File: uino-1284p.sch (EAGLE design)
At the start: 59 parts, among them J1 POWER, J2 POWER_JACKPTH, J3 M03X2, J4 POWER_SELECT, J5 M03X2, J6 IO, J7 ANALOG, J8 IOL, J9 IOH, U1 LD117AS50TR, U2 ATMEGA1284AU, U3 ATMEGA8U2AU, X1 16MHz, X2 16MHz

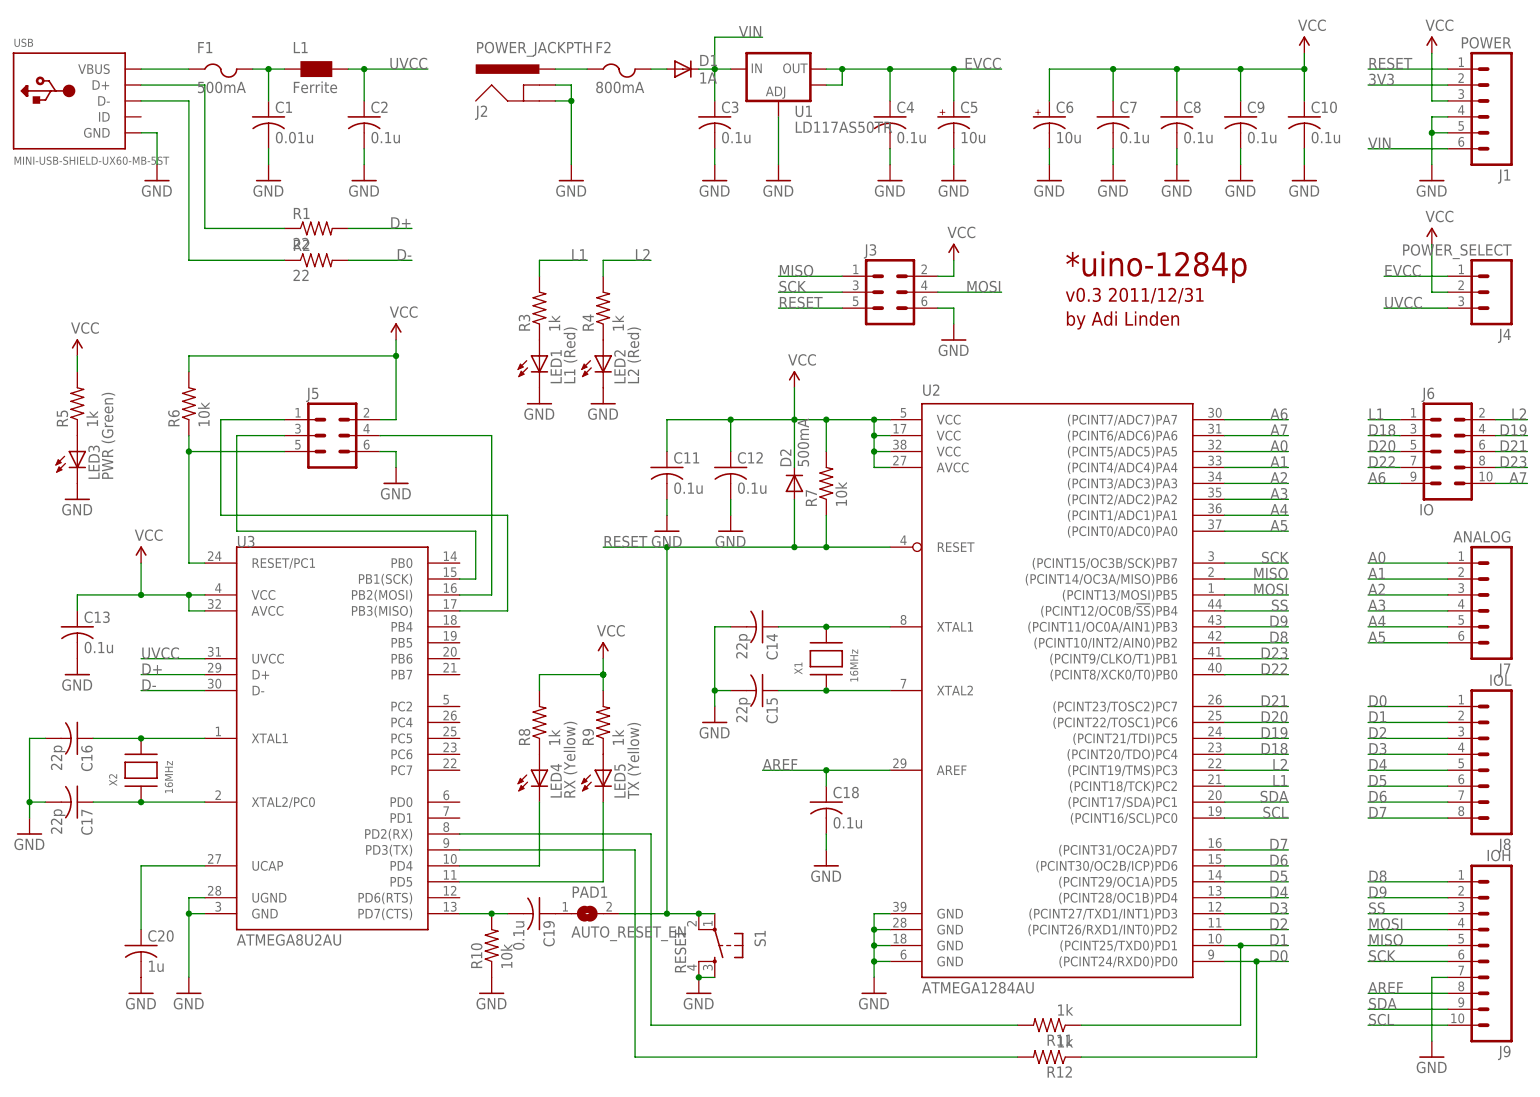
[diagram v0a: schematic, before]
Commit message: Unified device name text on board. Arranged name labels.
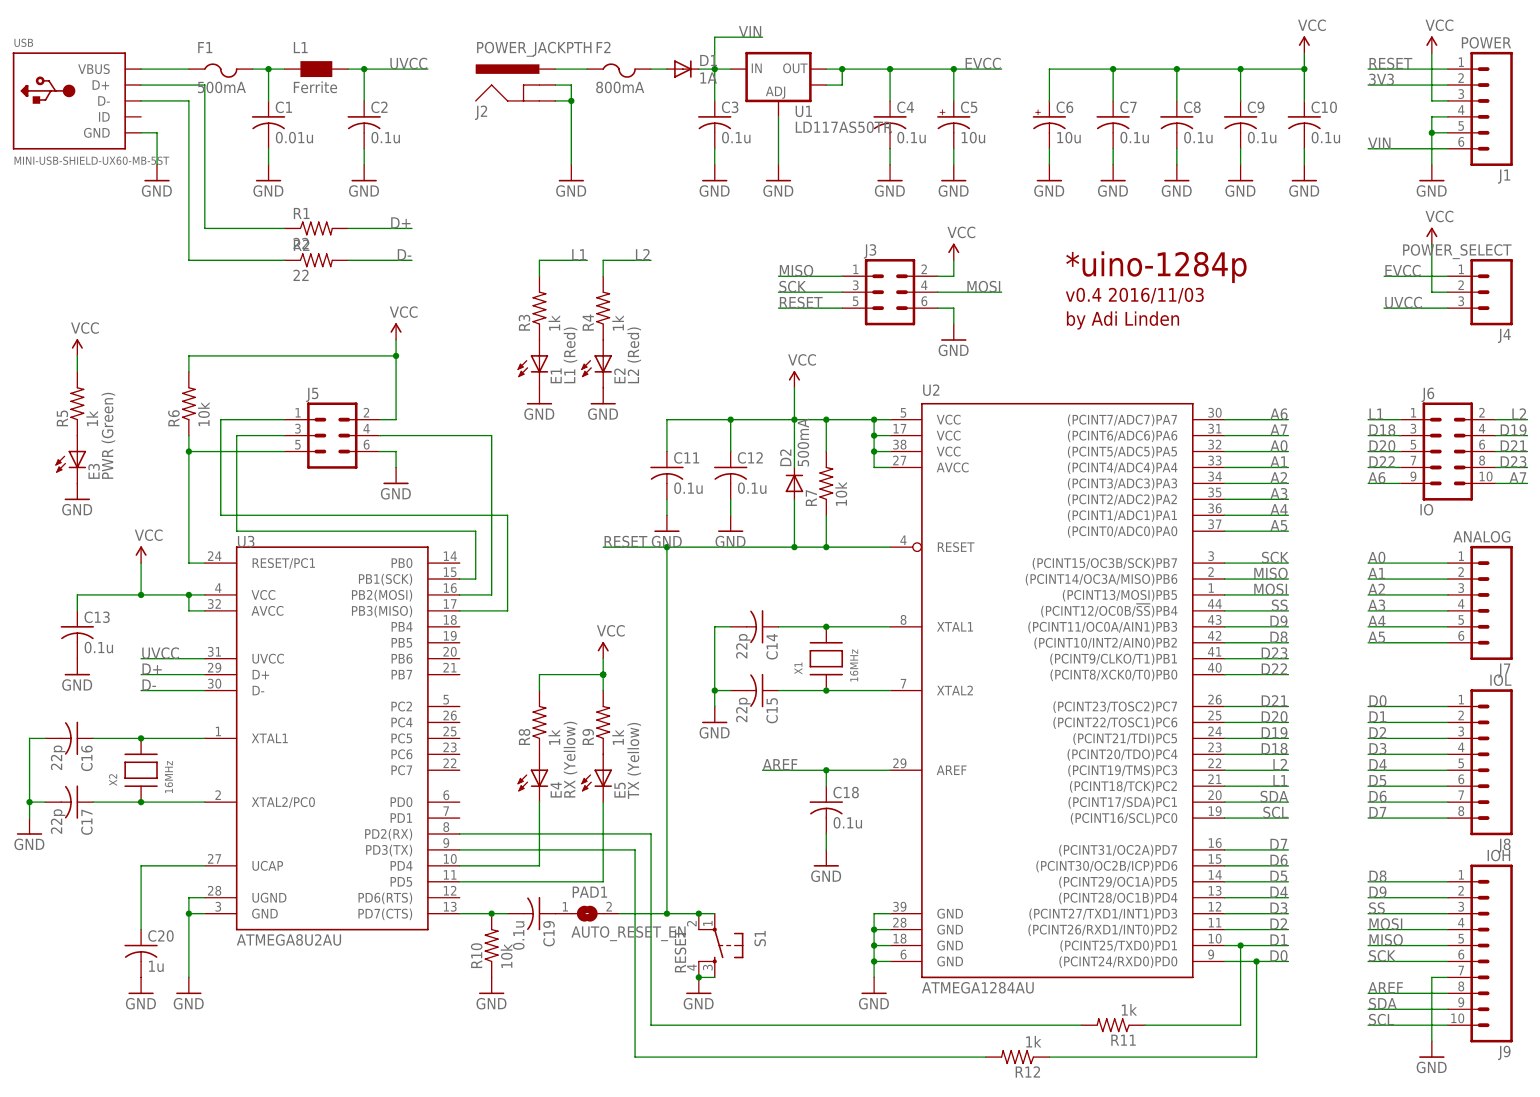
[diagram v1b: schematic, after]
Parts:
- renumbered LED1 to E1, LED2 to E2, LED3 to E3, LED4 to E4, LED5 to E5
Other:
- note added: "v0.4 2016/11/03"
- note removed: "v0.3 2011/12/31"
- moved on the sheet: R11, R12
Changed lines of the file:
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@@
 <setting verticaltext="up"/>
 </settings>
-<grid distance="0.1" unitdist="inch" unit="inch" style="lines" multiple="1" display="yes" altdistance="0.01" altunitdist="inch" altunit="inch"/>
+<grid distance="0.1" unitdist="inch" unit="inch" style="lines" multiple="1" display="no" altdistance="0.01" altunitdist="inch" altunit="inch"/>
 <layers>
 <layer number="1" name="Top" color="4" fill="1" visible="no" active="no"/>
@@
 <part name="P+3" library="SparkFun" deviceset="VCC" device=""/>
 <part name="GND12" library="supply1" deviceset="GND" device=""/>
-<part name="LED4" library="adafruit" deviceset="LED" device="CHIP-LED0805" value="RX (Yellow)"/>
-<part name="LED5" library="adafruit" deviceset="LED" device="CHIP-LED0805" value="TX (Yellow)"/>
+<part name="E4" library="adafruit" deviceset="LED" device="CHIP-LED0805" value="RX (Yellow)"/>
+<part name="E5" library="adafruit" deviceset="LED" device="CHIP-LED0805" value="TX (Yellow)"/>
 <part name="R8" library="rcl" deviceset="R-US_" device="R0805" value="1k"/>
 <part name="R9" library="rcl" deviceset="R-US_" device="R0805" value="1k"/>
@@
 <part name="C5" library="rcl" deviceset="CPOL-US" device="CT3216" value="10u"/>
 <part name="R5" library="rcl" deviceset="R-US_" device="R0805" value="1k"/>
-<part name="LED3" library="adafruit" deviceset="LED" device="CHIP-LED0805" value="PWR (Green)"/>
+<part name="E3" library="adafruit" deviceset="LED" device="CHIP-LED0805" value="PWR (Green)"/>
 <part name="GND19" library="supply1" deviceset="GND" device=""/>
 <part name="R7" library="rcl" deviceset="R-US_" device="R0805" value="10k"/>
@@
 <part name="P+7" library="SparkFun" deviceset="VCC" device=""/>
 <part name="R3" library="rcl" deviceset="R-US_" device="R0805" value="1k"/>
-<part name="LED1" library="adafruit" deviceset="LED" device="CHIP-LED0805" value="L1 (Red)"/>
+<part name="E1" library="adafruit" deviceset="LED" device="CHIP-LED0805" value="L1 (Red)"/>
 <part name="GND21" library="supply1" deviceset="GND" device=""/>
 <part name="R4" library="rcl" deviceset="R-US_" device="R0805" value="1k"/>
-<part name="LED2" library="adafruit" deviceset="LED" device="CHIP-LED0805" value="L2 (Red)"/>
+<part name="E2" library="adafruit" deviceset="LED" device="CHIP-LED0805" value="L2 (Red)"/>
 <part name="GND22" library="supply1" deviceset="GND" device=""/>
 <part name="P+9" library="SparkFun" deviceset="VCC" device=""/>
@@
 <plain>
 <text x="172.72" y="137.16" size="3.81" layer="94" ratio="18">*uino-1284p</text>
-<text x="172.72" y="133.096" size="2.1844" layer="94" ratio="12">v0.3 2011/12/31</text>
+<text x="172.72" y="133.096" size="2.1844" layer="94" ratio="12">v0.4 2016/11/03</text>
 <text x="172.72" y="129.286" size="2.1844" layer="94" ratio="12">by Adi Linden</text>
 </plain>
@@
 <instance part="P+3" gate="1" x="129.54" y="119.38"/>
 <instance part="GND12" gate="1" x="142.24" y="22.86"/>
-<instance part="LED4" gate="G$1" x="88.9" y="58.42"/>
-<instance part="LED5" gate="G$1" x="99.06" y="58.42"/>
+<instance part="E4" gate="G$1" x="88.9" y="58.42"/>
+<instance part="E5" gate="G$1" x="99.06" y="58.42"/>
 <instance part="R8" gate="G$1" x="88.9" y="66.04" rot="R90"/>
 <instance part="R9" gate="G$1" x="99.06" y="66.04" rot="R90"/>
@@
 <instance part="C5" gate="G$1" x="154.94" y="162.56"/>
 <instance part="R5" gate="G$1" x="15.24" y="116.84" rot="R90"/>
-<instance part="LED3" gate="G$1" x="15.24" y="109.22"/>
+<instance part="E3" gate="G$1" x="15.24" y="109.22"/>
 <instance part="GND19" gate="1" x="15.24" y="101.6"/>
 <instance part="R7" gate="G$1" x="134.62" y="104.14" rot="R90"/>
@@
 <instance part="GND20" gate="1" x="134.62" y="43.18"/>
 <instance part="S1" gate="S" x="116.84" y="30.48" rot="R270"/>
-<instance part="R11" gate="G$1" x="170.18" y="17.78" rot="R180"/>
-<instance part="R12" gate="G$1" x="170.18" y="12.7" rot="R180"/>
+<instance part="R11" gate="G$1" x="180.34" y="17.78" rot="R180"/>
+<instance part="R12" gate="G$1" x="165.1" y="12.7" rot="R180"/>
 <instance part="P+5" gate="1" x="15.24" y="124.46"/>
 <instance part="P+6" gate="1" x="231.14" y="172.72"/>
@@
 <instance part="P+7" gate="1" x="154.94" y="139.7"/>
 <instance part="R3" gate="G$1" x="88.9" y="132.08" rot="R90"/>
-<instance part="LED1" gate="G$1" x="88.9" y="124.46"/>
+<instance part="E1" gate="G$1" x="88.9" y="124.46"/>
 <instance part="GND21" gate="1" x="88.9" y="116.84"/>
 <instance part="R4" gate="G$1" x="99.06" y="132.08" rot="R90"/>
-<instance part="LED2" gate="G$1" x="99.06" y="124.46"/>
+<instance part="E2" gate="G$1" x="99.06" y="124.46"/>
 <instance part="GND22" gate="1" x="99.06" y="116.84"/>
 <instance part="P+9" gate="1" x="210.82" y="172.72"/>
@@
 </segment>
 <segment>
-<pinref part="LED3" gate="G$1" pin="C"/>
+<pinref part="E3" gate="G$1" pin="C"/>
 <pinref part="GND19" gate="1" pin="GND"/>
 </segment>
@@
 </segment>
 <segment>
-<pinref part="LED1" gate="G$1" pin="C"/>
+<pinref part="E1" gate="G$1" pin="C"/>
 <pinref part="GND21" gate="1" pin="GND"/>
 </segment>
 <segment>
-<pinref part="LED2" gate="G$1" pin="C"/>
+<pinref part="E2" gate="G$1" pin="C"/>
 <pinref part="GND22" gate="1" pin="GND"/>
 </segment>
@@
 <wire x1="198.12" y1="27.94" x2="203.2" y2="27.94" width="0.1524" layer="91"/>
 <wire x1="203.2" y1="27.94" x2="208.28" y2="27.94" width="0.1524" layer="91"/>
-<wire x1="175.26" y1="12.7" x2="203.2" y2="12.7" width="0.1524" layer="91"/>
+<wire x1="170.18" y1="12.7" x2="203.2" y2="12.7" width="0.1524" layer="91"/>
 <wire x1="203.2" y1="12.7" x2="203.2" y2="27.94" width="0.1524" layer="91"/>
 <junction x="203.2" y="27.94"/>
@@
 <wire x1="198.12" y1="30.48" x2="200.66" y2="30.48" width="0.1524" layer="91"/>
 <wire x1="200.66" y1="30.48" x2="208.28" y2="30.48" width="0.1524" layer="91"/>
-<wire x1="175.26" y1="17.78" x2="200.66" y2="17.78" width="0.1524" layer="91"/>
+<wire x1="185.42" y1="17.78" x2="200.66" y2="17.78" width="0.1524" layer="91"/>
 <wire x1="200.66" y1="17.78" x2="200.66" y2="30.48" width="0.1524" layer="91"/>
 <junction x="200.66" y="30.48"/>
@@
 <segment>
 <pinref part="R8" gate="G$1" pin="1"/>
-<pinref part="LED4" gate="G$1" pin="A"/>
+<pinref part="E4" gate="G$1" pin="A"/>
 </segment>
 </net>
@@
 <segment>
 <pinref part="R9" gate="G$1" pin="1"/>
-<pinref part="LED5" gate="G$1" pin="A"/>
+<pinref part="E5" gate="G$1" pin="A"/>
 </segment>
 </net>
@@
 <wire x1="88.9" y1="53.34" x2="88.9" y2="43.18" width="0.1524" layer="91"/>
 <wire x1="88.9" y1="43.18" x2="76.2" y2="43.18" width="0.1524" layer="91"/>
-<pinref part="LED4" gate="G$1" pin="C"/>
+<pinref part="E4" gate="G$1" pin="C"/>
 <pinref part="U3" gate="G$1" pin="PD4"/>
 </segment>
@@
 <wire x1="99.06" y1="40.64" x2="99.06" y2="53.34" width="0.1524" layer="91"/>
 <pinref part="U3" gate="G$1" pin="PD5"/>
-<pinref part="LED5" gate="G$1" pin="C"/>
+<pinref part="E5" gate="G$1" pin="C"/>
 </segment>
 </net>
@@
 <segment>
 <pinref part="R5" gate="G$1" pin="1"/>
-<pinref part="LED3" gate="G$1" pin="A"/>
+<pinref part="E3" gate="G$1" pin="A"/>
 </segment>
 </net>
@@
 <wire x1="76.2" y1="45.72" x2="104.14" y2="45.72" width="0.1524" layer="91"/>
 <wire x1="104.14" y1="45.72" x2="104.14" y2="12.7" width="0.1524" layer="91"/>
-<wire x1="104.14" y1="12.7" x2="165.1" y2="12.7" width="0.1524" layer="91"/>
+<wire x1="104.14" y1="12.7" x2="160.02" y2="12.7" width="0.1524" layer="91"/>
 <pinref part="U3" gate="G$1" pin="PD3(TX)"/>
 <pinref part="R12" gate="G$1" pin="2"/>
@@
 <wire x1="76.2" y1="48.26" x2="106.68" y2="48.26" width="0.1524" layer="91"/>
 <wire x1="106.68" y1="48.26" x2="106.68" y2="17.78" width="0.1524" layer="91"/>
-<wire x1="106.68" y1="17.78" x2="165.1" y2="17.78" width="0.1524" layer="91"/>
+<wire x1="106.68" y1="17.78" x2="175.26" y2="17.78" width="0.1524" layer="91"/>
 <pinref part="U3" gate="G$1" pin="PD2(RX)"/>
 <pinref part="R11" gate="G$1" pin="2"/>
@@
 <segment>
 <pinref part="R3" gate="G$1" pin="1"/>
-<pinref part="LED1" gate="G$1" pin="A"/>
+<pinref part="E1" gate="G$1" pin="A"/>
 </segment>
 </net>
@@
 <segment>
 <pinref part="R4" gate="G$1" pin="1"/>
-<pinref part="LED2" gate="G$1" pin="A"/>
-</segment>
-</net>
+<pinref part="E2" gate="G$1" pin="A"/>
+</segment>
+</net>
